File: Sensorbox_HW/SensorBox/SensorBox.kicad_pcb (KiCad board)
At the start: 2 copper layers, 128.5 x 97.5 mm, 81 parts, among them U1 BME280, U11 PS1-O3-100, U12 DS3231M, U13 OPA197xD, U2 OPA197xD, U4 MC33063AD, U5 OPA197xD, U6 MAX31855EASA, U8 HPP845E131R5

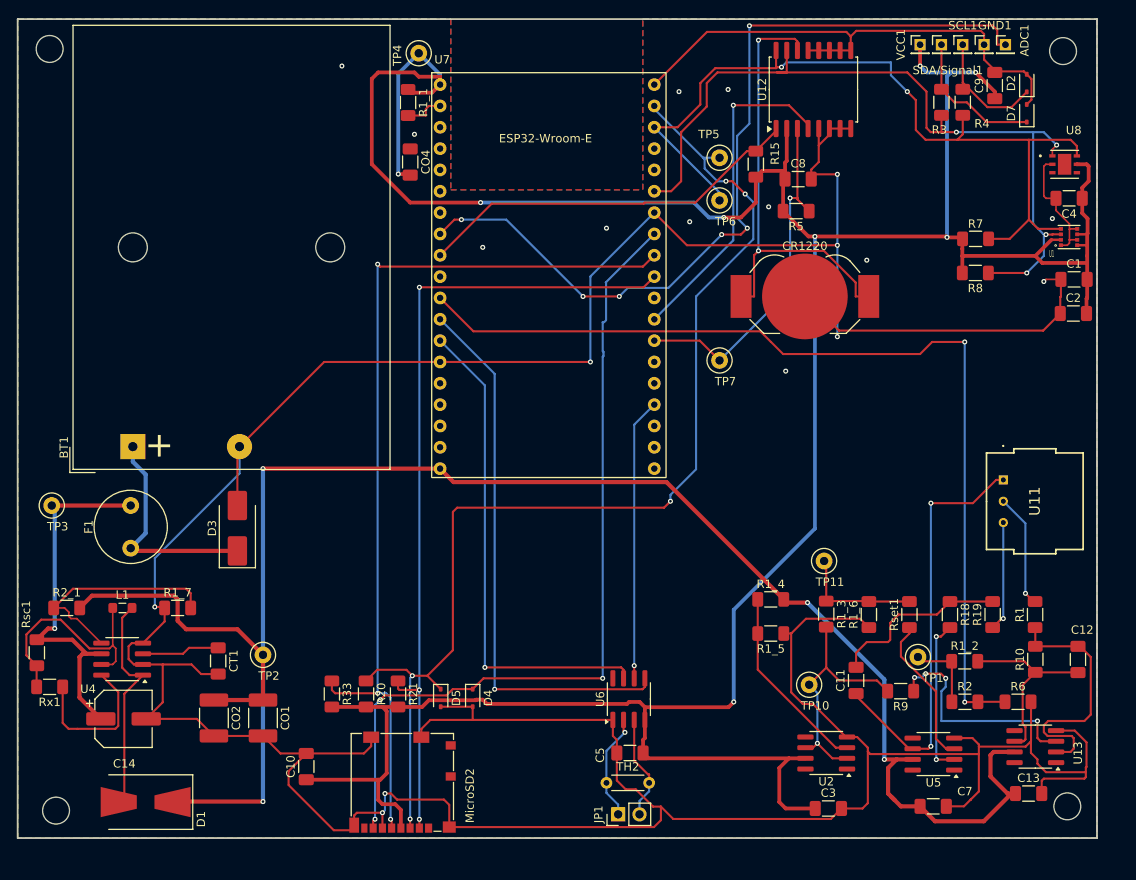
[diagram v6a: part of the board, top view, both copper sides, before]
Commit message: Layout, Schaltplan, Doku
Footprint von L1 abgeändert, Doku weitergearbeitet
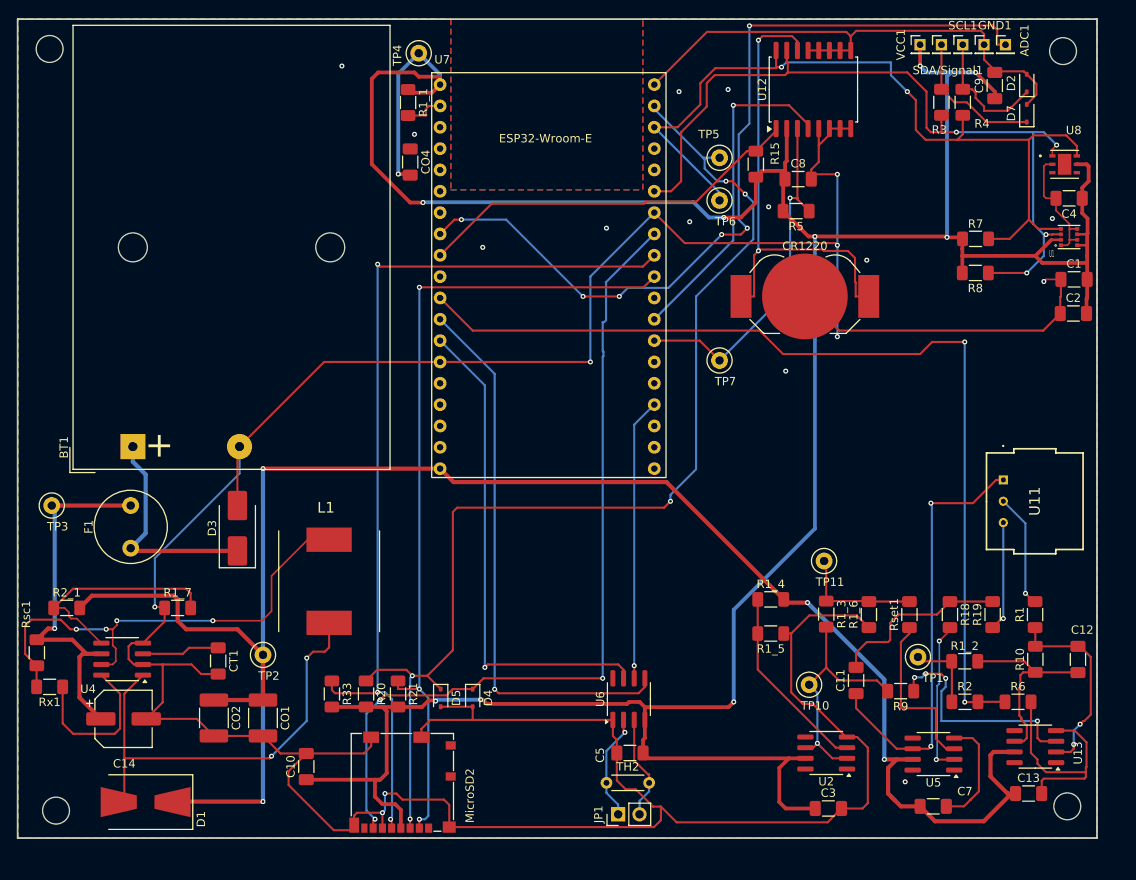
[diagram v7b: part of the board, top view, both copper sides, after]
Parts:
- CT1: value 1500pF -> 1500pF - 50V
- L1: value 56µH - 2.1A -> 56 uH - 2.1A; footprint Inductor_SMD:L_0805_2012Metric_Pad1.05x1.20mm_HandSolder -> L1_Spule:L1
- moved L1 24.8 mm to (49.0, 78.9), turned to -90 degrees
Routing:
- net Net-(U4-Ipk): track 28.1 -> 58.2 mm, vias 0 -> 4
- net Net-(D1-A): track 26.7 -> 53.5 mm, vias 0 -> 2
- net GND1: track 565.9 -> 547.3 mm, vias 19 -> 20
- net Net-(U13--): track 30.3 -> 23.2 mm, vias 0 -> 2
- net Net-(U5-+): track 18.0 -> 20.5 mm
- net Net-(CR1220-+): track 54.7 -> 56.7 mm
- net Net-(C12-Pad2): track 22.7 -> 24.0 mm
- net CS_GPIO5: track 96.4 -> 97.6 mm
- net SDA_GPIO21: track 97.0 -> 95.9 mm
- net Net-(U4-DC): track 18.2 -> 19.2 mm
- net Net-(C11-Pad1): track 50.6 -> 51.6 mm
- net Miso_GPIO19: track 98.8 -> 99.7 mm
- net Net-(D2-K): track 14.9 -> 15.6 mm
- net VDD_3V3: track 382.6 -> 382.8 mm, vias 8 -> 10

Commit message: Finales Layout angefangen
.
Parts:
- removed the ADC1 at (129.5, 15.0)
- removed the GND1 at (127.0, 15.0)
- removed the SCL1 at (124.5, 15.0)
- removed the SDA/Signal1 at (121.9, 15.0)
- removed TP5, TP6, TP7: TestPoint, TestPoint:TestPoint_Loop_D1.80mm_Drill1.0mm_Beaded
- removed the VCC1 at (119.4, 15.0)
- added ADC1: Conn_01x01_Socket, Connector_PinHeader_2.00mm:PinHeader_1x01_P2.00mm_Vertical, F.Cu at (76.5, 34.7)
- added ADC1: Conn_01x01_Socket, Connector_PinHeader_2.00mm:PinHeader_1x01_P2.00mm_Vertical, F.Cu at (-30.8, 60.6)
- added GND1: Conn_01x01_Socket, Connector_PinHeader_2.00mm:PinHeader_1x01_P2.00mm_Vertical, F.Cu at (76.5, 32.1)
- added GND1: Conn_01x01_Socket, Connector_PinHeader_2.00mm:PinHeader_1x01_P2.00mm_Vertical, F.Cu at (-30.8, 64.7)
- added R2_2: 47k, Resistor_SMD:R_1206_3216Metric_Pad1.30x1.75mm_HandSolder, F.Cu at (35.9, 30.4)
- added SCL1: Conn_01x01_Socket, Connector_PinHeader_2.00mm:PinHeader_1x01_P2.00mm_Vertical, F.Cu at (-30.8, 68.7)
- added SCL1: Conn_01x01_Socket, Connector_PinHeader_2.00mm:PinHeader_1x01_P2.00mm_Vertical, F.Cu at (76.5, 29.6)
- added SDA/Signal1: Conn_01x01_Socket, Connector_PinHeader_2.00mm:PinHeader_1x01_P2.00mm_Vertical, F.Cu at (-30.8, 73.2)
- added SDA/Signal1: Conn_01x01_Socket, Connector_PinHeader_2.00mm:PinHeader_1x01_P2.00mm_Vertical, F.Cu at (76.5, 27.1)
- added VCC1: Conn_01x01_Socket, Connector_PinHeader_2.00mm:PinHeader_1x01_P2.00mm_Vertical, F.Cu at (-30.8, 76.8)
- added VCC1: Conn_01x01_Socket, Connector_PinHeader_2.00mm:PinHeader_1x01_P2.00mm_Vertical, F.Cu at (76.5, 24.5)
- BT1, C10, C8, CR1220, D4, D5, MicroSD2, R15, R20, R21, R33, R5, U12, U7: moved to B.Cu
- moved R1 200.0 mm to (-65.6, 60.2), turned to 0 degrees
- moved R6 197.4 mm to (-65.6, 76.7)
- moved R10 194.0 mm to (-59.7, 66.8), turned to 0 degrees
- moved R2 192.7 mm to (-65.6, 63.5)
- moved R19 187.8 mm to (-59.7, 76.7), turned to 0 degrees
- moved R18 182.9 mm to (-59.7, 73.4), turned to 0 degrees
- moved R1_2 179.4 mm to (-53.7, 70.1)
- moved U13 179.0 mm to (-38.9, 48.9), turned to 0 degrees
- moved R9 179.0 mm to (-59.7, 63.5), turned to 0 degrees
- moved C12 174.9 mm to (-35.8, 70.3), turned to 0 degrees
- moved U5 172.1 mm to (-38.9, 35.8), turned to 0 degrees
- moved C13 170.8 mm to (-35.8, 73.7)
- moved Rset1 166.0 mm to (-47.8, 76.7), turned to 0 degrees
- moved U2 165.9 mm to (-38.9, 22.6), turned to 0 degrees
- moved C7 165.3 mm to (-41.8, 77.0)
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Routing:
- net GND1: track 547.3 -> 0.00 mm, vias 20 -> 0
- net VDD_3V3: track 382.8 -> 5.35 mm, vias 10 -> 0
- net VDD_5V: track 217.6 -> 0.00 mm, vias 4 -> 0
- net Mosi_GPIO23: track 134.9 -> 0.00 mm, vias 5 -> 0
- net Ozon_out_ADC_GPIO27: track 113.5 -> 0.00 mm, vias 2 -> 0
- net SCK_GPIO18: track 108.8 -> 0.00 mm, vias 3 -> 0
- net extern_Sensor_Gpio_33: track 101.9 -> 0.00 mm, vias 6 -> 0
- net Miso_GPIO19: track 99.7 -> 0.00 mm, vias 3 -> 0
- net CS_GPIO5: track 97.6 -> 0.00 mm, vias 3 -> 0
- net SCK_GPIO14: track 66.1 -> 0.00 mm, vias 1 -> 0
- net Miso_GPIO12: track 59.0 -> 0.00 mm, vias 1 -> 0
- net Net-(U4-Ipk): track 58.2 -> 0.00 mm, vias 4 -> 0
- net Net-(CR1220-+): track 56.7 -> 0.00 mm, vias 2 -> 0
- net Net-(D1-A): track 53.5 -> 0.00 mm, vias 2 -> 0
- net Net-(C11-Pad1): track 51.6 -> 0.00 mm, vias 2 -> 0
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- removed copper zone on B.Cu, net GND1
- removed copper zone on F.Cu, net GND1
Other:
- board outline removed
